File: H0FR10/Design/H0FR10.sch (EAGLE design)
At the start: 26 parts, among them J1 CON-PHOENIX-350_1755749, K1 G5LE-14_DC3, P1 HEXABIT_17.32_NO_P6, Q1 MMBT3904LT1, U1 STM32F091CBU6, X1 XTALL_CSTCE8M00G52

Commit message: Fixed R2 PN
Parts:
- R2: MFN Yageo -> Panasonic; MPN RC0402FR-07100RL -> ERJ-3GEYJ181V
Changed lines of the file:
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@@
 <part name="D3" library="Hexabitz" deviceset="SMD-DIODE-SCHOTTKY-40V-300MA(SOD-323)" device=""/>
 <part name="R2" library="Hexabitz" deviceset="R-0603" device="" value="180.0 Ω">
-<attribute name="MFN" value="Yageo"/>
-<attribute name="MPN" value="RC0402FR-07100RL"/>
+<attribute name="MFN" value="Panasonic"/>
+<attribute name="MPN" value="ERJ-3GEYJ181V"/>
 <attribute name="OCTOPART_URL" value="https://octopart.com/erj-3geyj181v-panasonic-55403673"/>
 <attribute name="RESISTANCE" value="180.0 Ω"/>

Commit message: editing notes & descriptions (3oz to 2oz  & 10A to 8A)
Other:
- note added: "8A SPDT Relay"
- note removed: "10A SPDT Relay"
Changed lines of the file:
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@@
 <?xml version="1.0" encoding="utf-8"?>
 <!DOCTYPE eagle SYSTEM "eagle.dtd">
-<eagle version="9.3.0">
+<eagle version="9.6.0">
 <drawing>
 <settings>
@@
 <setting verticaltext="up"/>
 </settings>
-<grid distance="5" unitdist="mil" unit="mil" style="lines" multiple="1" display="no" altdistance="0.01" altunitdist="inch" altunit="inch"/>
+<grid distance="0.1" unitdist="inch" unit="inch" style="lines" multiple="1" display="no" altdistance="0.01" altunitdist="inch" altunit="inch"/>
 <layers>
 <layer number="1" name="Top" color="4" fill="1" visible="no" active="no"/>
@@
 <text x="199.4662" y="19.6342" size="1.9304" layer="100" font="vector">Title</text>
 <text x="180.9242" y="19.6342" size="1.9304" layer="102" font="vector">H0FR10</text>
-<text x="179.2478" y="11.2014" size="1.9304" layer="101" font="vector">10A SPDT Relay </text>
+<text x="179.2478" y="11.2014" size="1.9304" layer="101" font="vector">8A SPDT Relay </text>
 <text x="206.3242" y="19.6342" size="1.9304" layer="101" font="vector">H0FR10_Backend</text>
 <wire x1="168.91" y1="3.81" x2="168.91" y2="8.128" width="0.1524" layer="205"/>
@@
 <text x="199.4662" y="19.6342" size="1.9304" layer="100" font="vector">Title</text>
 <text x="180.9242" y="19.6342" size="1.9304" layer="102" font="vector">H0FR10</text>
-<text x="179.2478" y="11.2014" size="1.9304" layer="101" font="vector">10A SPDT Relay </text>
+<text x="179.2478" y="11.2014" size="1.9304" layer="101" font="vector">8A SPDT Relay </text>
 <text x="206.3242" y="19.6342" size="1.9304" layer="101" font="vector">H0FR10_Frontend</text>
 <wire x1="168.91" y1="3.81" x2="168.91" y2="8.128" width="0.1524" layer="205"/>

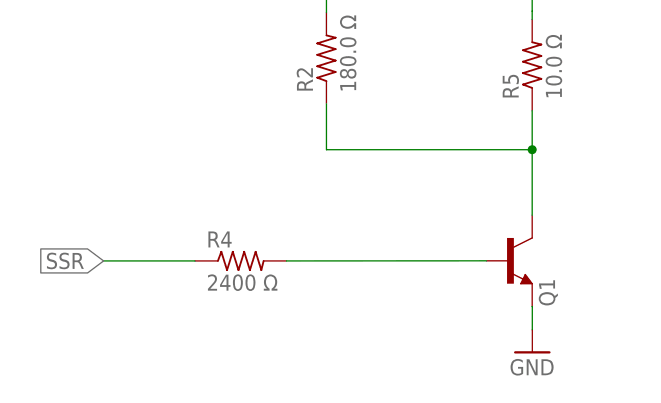
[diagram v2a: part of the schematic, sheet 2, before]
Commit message: change base resistor(R4) from 2k4 to 1k0 Schematic & BOM was changed
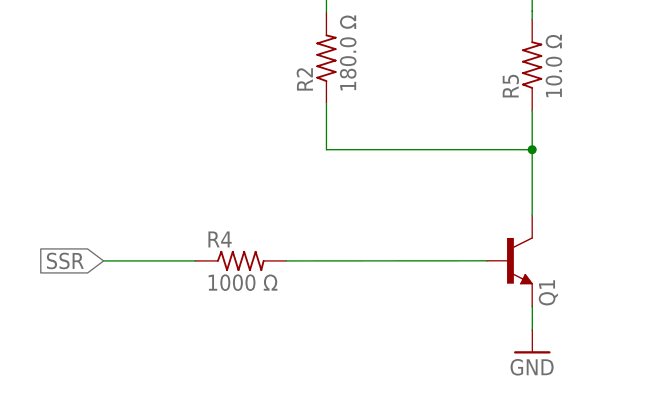
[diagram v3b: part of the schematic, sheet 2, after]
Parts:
- R4: value 2400 Ω -> 1000 Ω; MPN RC0603JR-070RL -> CRCW06031K00JNEA; OCTOPART_URL https://octopart.com/crcw06032k40jnea-vishay-40298967 -> https://octopart.com/crcw06031k00jnea-vishay-55388219?r=sp; RESISTANCE 2400.0 Ω -> 1000.0 Ω
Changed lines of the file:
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@@
 <?xml version="1.0" encoding="utf-8"?>
 <!DOCTYPE eagle SYSTEM "eagle.dtd">
-<eagle version="9.6.0">
+<eagle version="9.6.1">
 <drawing>
 <settings>
@@
 <attribute name="VOLTAGE_RATING_DC" value="40.0 V"/>
 </part>
-<part name="R4" library="Hexabitz" deviceset="R-0603" device="" value="2400 Ω">
+<part name="R4" library="Hexabitz" deviceset="R-0603" device="" value="1000 Ω">
 <attribute name="MFN" value="Yageo"/>
-<attribute name="MPN" value="RC0603JR-070RL"/>
-<attribute name="OCTOPART_URL" value="https://octopart.com/crcw06032k40jnea-vishay-40298967"/>
-<attribute name="RESISTANCE" value="2400.0 Ω"/>
+<attribute name="MPN" value="CRCW06031K00JNEA"/>
+<attribute name="OCTOPART_URL" value="https://octopart.com/crcw06031k00jnea-vishay-55388219?r=sp"/>
+<attribute name="RESISTANCE" value="1000.0 Ω"/>
 <attribute name="TOLERANCE" value="±5%"/>
 </part>

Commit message: Fix ERC errors Generate PDF Release at V0 again
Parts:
- R4: MFN Yageo -> Vishay
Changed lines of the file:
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@@
 </part>
 <part name="R4" library="Hexabitz" deviceset="R-0603" device="" value="1000 Ω">
-<attribute name="MFN" value="Yageo"/>
+<attribute name="MFN" value="Vishay"/>
 <attribute name="MPN" value="CRCW06031K00JNEA"/>
 <attribute name="OCTOPART_URL" value="https://octopart.com/crcw06031k00jnea-vishay-55388219?r=sp"/>
